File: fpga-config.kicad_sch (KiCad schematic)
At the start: 15 parts, among them J2 Tag-Connect_TC2050-IDC-NL_2x5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, U1 MPFS250T-FCVG484, U3 MT25QL01GBBB1EW9-0SIT

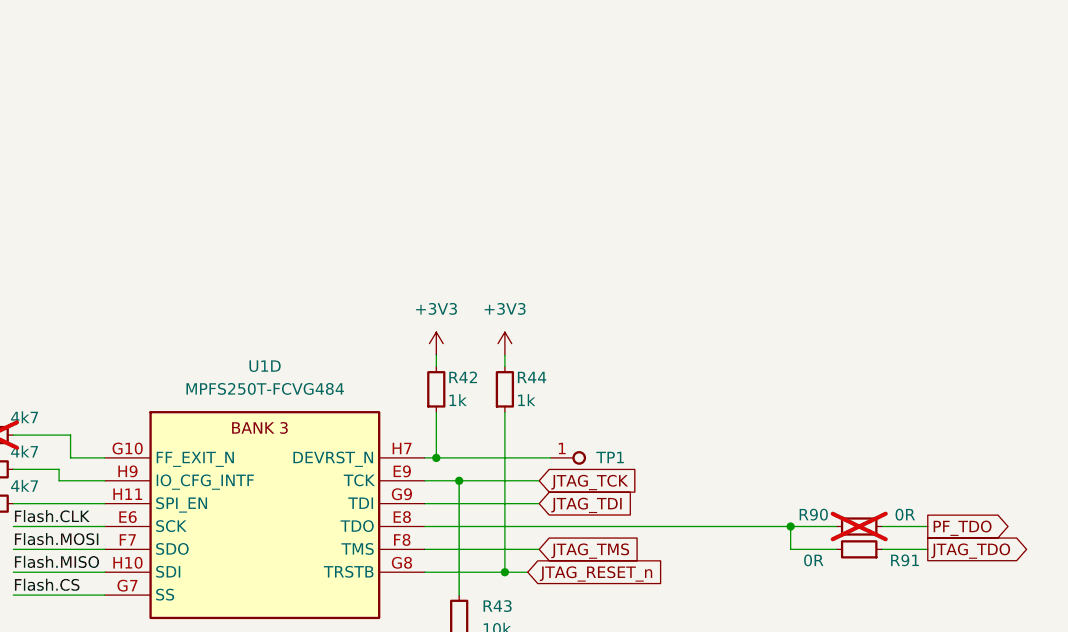
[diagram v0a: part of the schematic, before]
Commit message: [#76827] Update PolarFire MPN. Add test points. Modify DEVRST_N sequence. Bump revision
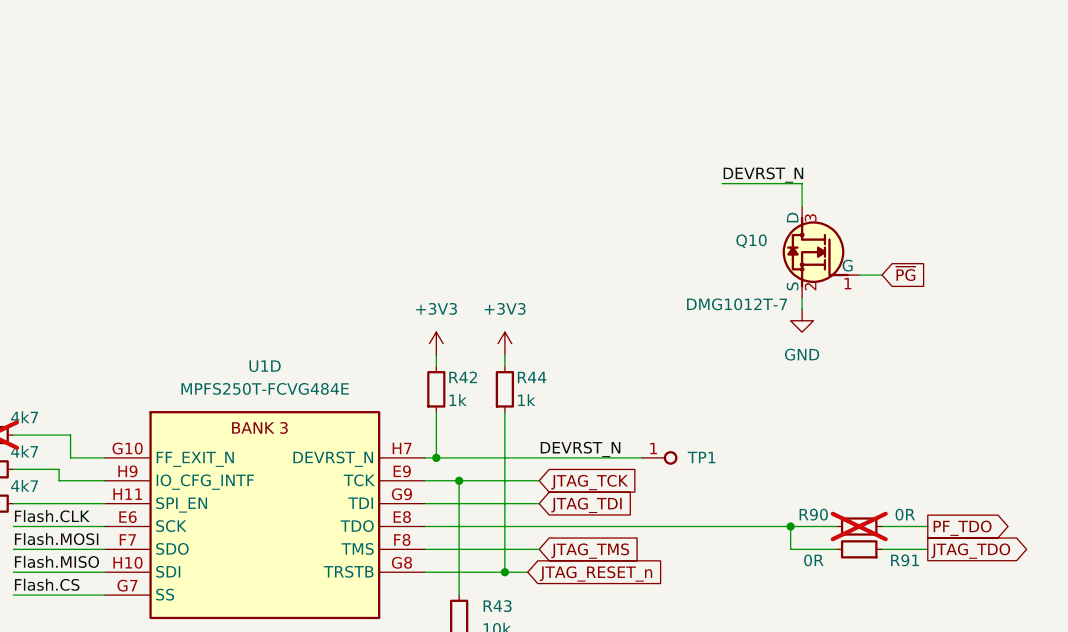
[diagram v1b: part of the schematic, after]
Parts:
- added Q10: DMG1012T-7, antmicro-footprints:SOT-523, symbol antmicroTransistorsFETsMOSFETsSingle:DMG1012T-7
- U1: footprint antmicro-footprints:BGA-484_19x19mm_Layout22x22_P0.8mm-microchip-technology-mpfs250t-fcvg484 -> antmicro-footprints:BGA-484_19x19mm_Layout22x22_P0.8mm_FCVG484; symbol antmicroFPGAChips:MPFS250T-FCVG484 -> antmicroFPGAChips:MPFS250T-FCVG484E; MPN MPFS250T-FCVG484 -> MPFS250T-FCVG484E
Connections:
- net GND: now also Q10.2 (S)
- net DEVRST_N: now reaches R42.1, TP1.1, U1.H7 (DEVRST_N)
- net DEVRST_N: now also Q10.3 (D)
- new net ~{PG}: Q10.1 (G)
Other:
- moved on the sheet: TP1
